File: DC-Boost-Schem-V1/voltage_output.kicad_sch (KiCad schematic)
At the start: 12 parts, among them Q5 HCNR200-300E, U11 MCP6007, U12 MCP6007

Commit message: Worked on layout
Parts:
- renumbered C40 to C59, C41 to C60, C42 to C61, C43 to C62, Q5 to Q8, R28 to R43, R29 to R44, R30 to R45, R31 to R46, R32 to R47, U11 to U17, U12 to U18
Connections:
- net GNDD renamed GND

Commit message: Layout update
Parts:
- R46: footprint Resistor_SMD:R_0805_2012Metric -> Resistor_SMD:R_0603_1608Metric
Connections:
- net GNDPWR renamed GNDREF
- net GNDREF: no longer C59.1, U17.4 (V-)
- new net: C59.1, U17.4 (V-)

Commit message: update
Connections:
- net GNDREF: now also C59.1, U17.4 (V-)
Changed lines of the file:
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@@
+	)
+	(symbol
+		(lib_id "power:GNDREF")
+		(at 134.62 74.93 0)
+		(unit 1)
+		(exclude_from_sim no)
+		(in_bom yes)
+		(on_board yes)
+		(dnp no)
+		(fields_autoplaced yes)
+		(property "Reference" "#PWR0501"
+			(at 134.62 81.28 0)
+			(effects
+				(font
+					(size 1.27 1.27)
+				)
+				(hide yes)
+			)
+		)
+		(property "Value" "GNDREF"
+			(at 134.62 80.01 0)
+			(effects
+				(font
+					(size 1.27 1.27)
+				)
+			)
+		)
+		(property "Footprint" ""
+			(at 134.62 74.93 0)
+			(effects
+				(font
+					(size 1.27 1.27)
+				)
+				(hide yes)
+			)
+		)
+		(property "Datasheet" ""
+			(at 134.62 74.93 0)
+			(effects
+				(font
+					(size 1.27 1.27)
+				)
+				(hide yes)
+			)
+		)
+		(property "Description" "Power symbol creates a global label with name \"GNDREF\" , reference supply ground"
+			(at 134.62 74.93 0)
+			(effects
+				(font
+					(size 1.27 1.27)
+				)
+				(hide yes)
+			)
+		)
+		(pin "1"
+		)
+		(instances
+			(project "DC-DC-Boost-V1"
+				(path "/892bc44b-f7f8-4677-bf53-06d5523b6450/75fe99dd-6331-41c4-aaf2-0a4fa01a955e"
+					(reference "#PWR0501")
+					(unit 1)
+				)
+			)
+		)
 	)
 	(symbol

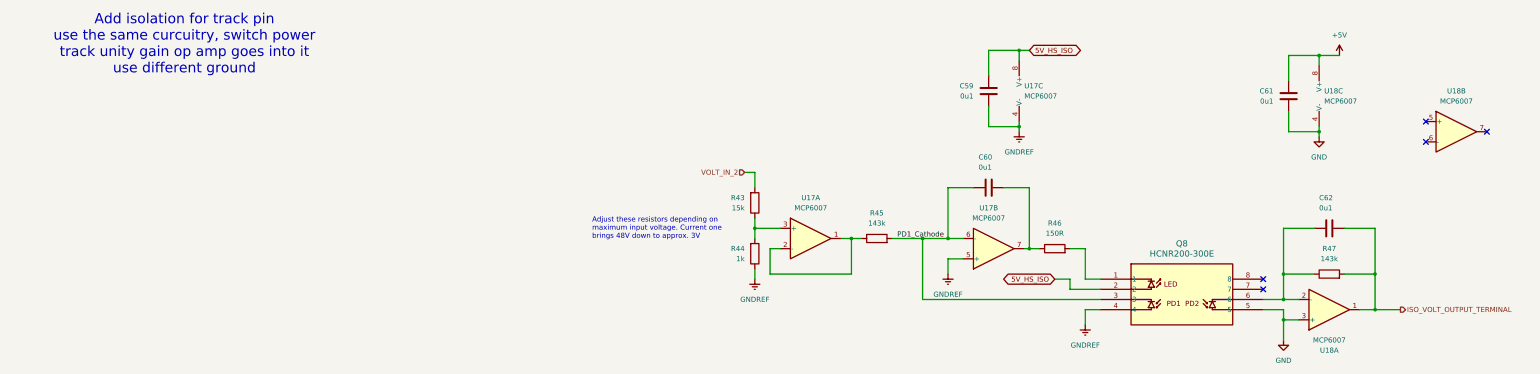
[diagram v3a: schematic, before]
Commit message: More layout and routing
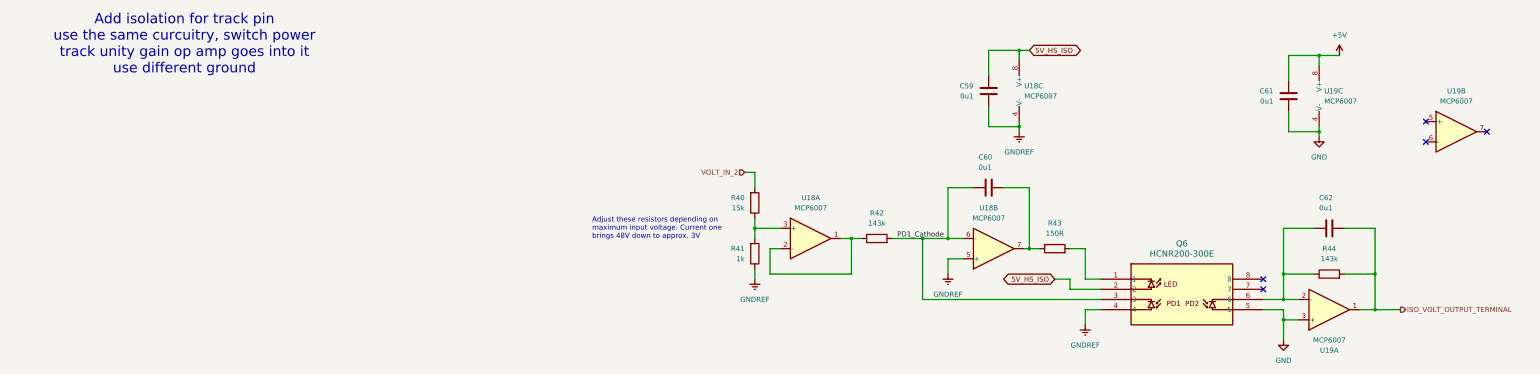
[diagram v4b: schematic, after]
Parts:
- renumbered Q8 to Q6, R43 to R40, R44 to R41, R45 to R42, R46 to R43, R47 to R44, U17 to U18, U18 to U19
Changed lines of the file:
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@@
 		(dnp no)
 		(fields_autoplaced yes)
-		(property "Reference" "#PWR079"
+		(property "Reference" "#PWR078"
 			(at 116.84 116.84 0)
 			(effects
@@
 			(project "DC-DC-Boost-V1"
 				(path "/892bc44b-f7f8-4677-bf53-06d5523b6450/75fe99dd-6331-41c4-aaf2-0a4fa01a955e"
-					(reference "#PWR079")
+					(reference "#PWR078")
 					(unit 1)
 				)
@@
 		(dnp no)
 		(fields_autoplaced yes)
-		(property "Reference" "Q8"
+		(property "Reference" "Q6"
 			(at 175.26 102.87 0)
 			(effects
@@
 			(project "DC-DC-Boost-V1"
 				(path "/892bc44b-f7f8-4677-bf53-06d5523b6450/75fe99dd-6331-41c4-aaf2-0a4fa01a955e"
-					(reference "Q8")
+					(reference "Q6")
 					(unit 1)
 				)
@@
 		(dnp no)
 		(fields_autoplaced yes)
-		(property "Reference" "R46"
+		(property "Reference" "R43"
 			(at 143.51 97.79 90)
 			(effects
@@
 			(project "DC-DC-Boost-V1"
 				(path "/892bc44b-f7f8-4677-bf53-06d5523b6450/75fe99dd-6331-41c4-aaf2-0a4fa01a955e"
-					(reference "R46")
+					(reference "R43")
 					(unit 1)
 				)
@@
 		(dnp no)
 		(fields_autoplaced yes)
-		(property "Reference" "#PWR085"
+		(property "Reference" "#PWR083"
 			(at 214.63 59.69 0)
 			(effects
@@
 			(project "DC-DC-Boost-V1"
 				(path "/892bc44b-f7f8-4677-bf53-06d5523b6450/75fe99dd-6331-41c4-aaf2-0a4fa01a955e"
-					(reference "#PWR085")
+					(reference "#PWR083")
 					(unit 1)
 				)
@@
 		(dnp no)
 		(fields_autoplaced yes)
-		(property "Reference" "#PWR099"
+		(property "Reference" "#PWR081"
 			(at 200.66 133.35 0)
 			(effects
@@
 			(project "DC-DC-Boost-V1"
 				(path "/892bc44b-f7f8-4677-bf53-06d5523b6450/75fe99dd-6331-41c4-aaf2-0a4fa01a955e"
-					(reference "#PWR099")
+					(reference "#PWR081")
 					(unit 1)
 				)
@@
 		(dnp no)
 		(fields_autoplaced yes)
-		(property "Reference" "R47"
+		(property "Reference" "R44"
 			(at 212.09 104.14 90)
 			(effects
@@
 			(project "DC-DC-Boost-V1"
 				(path "/892bc44b-f7f8-4677-bf53-06d5523b6450/75fe99dd-6331-41c4-aaf2-0a4fa01a955e"
-					(reference "R47")
+					(reference "R44")
 					(unit 1)
 				)
@@
 		(dnp no)
 		(fields_autoplaced yes)
-		(property "Reference" "#PWR0501"
+		(property "Reference" "#PWR079"
 			(at 134.62 81.28 0)
 			(effects
@@
 			(project "DC-DC-Boost-V1"
 				(path "/892bc44b-f7f8-4677-bf53-06d5523b6450/75fe99dd-6331-41c4-aaf2-0a4fa01a955e"
-					(reference "#PWR0501")
+					(reference "#PWR079")
 					(unit 1)
 				)
@@
 		(dnp no)
 		(fields_autoplaced yes)
-		(property "Reference" "U18"
+		(property "Reference" "U19"
 			(at 243.84 64.77 0)
 			(effects
@@
 			(project "DC-DC-Boost-V1"
 				(path "/892bc44b-f7f8-4677-bf53-06d5523b6450/75fe99dd-6331-41c4-aaf2-0a4fa01a955e"
-					(reference "U18")
+					(reference "U19")
 					(unit 2)
 				)
@@
 		(on_board yes)
 		(dnp no)
-		(property "Reference" "U18"
+		(property "Reference" "U19"
 			(at 212.09 129.54 0)
 			(effects
@@
 			(project "DC-DC-Boost-V1"
 				(path "/892bc44b-f7f8-4677-bf53-06d5523b6450/75fe99dd-6331-41c4-aaf2-0a4fa01a955e"
-					(reference "U18")
+					(reference "U19")
 					(unit 1)
 				)
@@
 		(dnp no)
 		(fields_autoplaced yes)
-		(property "Reference" "#PWR077"
+		(property "Reference" "#PWR082"
 			(at 209.55 82.55 0)
 			(effects
@@
 			(project "DC-DC-Boost-V1"
 				(path "/892bc44b-f7f8-4677-bf53-06d5523b6450/75fe99dd-6331-41c4-aaf2-0a4fa01a955e"
-					(reference "#PWR077")
+					(reference "#PWR082")
 					(unit 1)
 				)
@@
 		(dnp no)
 		(fields_autoplaced yes)
-		(property "Reference" "U18"
+		(property "Reference" "U19"
 			(at 210.82 64.7699 0)
 			(effects
@@
 			(project "DC-DC-Boost-V1"
 				(path "/892bc44b-f7f8-4677-bf53-06d5523b6450/75fe99dd-6331-41c4-aaf2-0a4fa01a955e"
-					(reference "U18")
+					(reference "U19")
 					(unit 3)
 				)
@@
 		(on_board yes)
 		(dnp no)
-		(property "Reference" "U17"
+		(property "Reference" "U18"
 			(at 127 93.98 0)
 			(effects
@@
 			(project "DC-DC-Boost-V1"
 				(path "/892bc44b-f7f8-4677-bf53-06d5523b6450/75fe99dd-6331-41c4-aaf2-0a4fa01a955e"
-					(reference "U17")
+					(reference "U18")
 					(unit 2)
 				)
@@
 		(dnp no)
 		(fields_autoplaced yes)
-		(property "Reference" "#PWR064"
+		(property "Reference" "#PWR077"
 			(at 68.58 118.11 0)
 			(effects
@@
 			(project "DC-DC-Boost-V1"
 				(path "/892bc44b-f7f8-4677-bf53-06d5523b6450/75fe99dd-6331-41c4-aaf2-0a4fa01a955e"
-					(reference "#PWR064")
+					(reference "#PWR077")
 					(unit 1)
 				)
@@
 		(on_board yes)
 		(dnp no)
-		(property "Reference" "R44"
+		(property "Reference" "R41"
 			(at 66.04 104.1399 0)
 			(effects
@@
 			(project "DC-DC-Boost-V1"
 				(path "/892bc44b-f7f8-4677-bf53-06d5523b6450/75fe99dd-6331-41c4-aaf2-0a4fa01a955e"
-					(reference "R44")
+					(reference "R41")
 					(unit 1)
 				)
@@
 		(dnp no)
 		(fields_autoplaced yes)
-		(property "Reference" "R45"
+		(property "Reference" "R42"
 			(at 99.06 95.25 90)
 			(effects
@@
 			(project "DC-DC-Boost-V1"
 				(path "/892bc44b-f7f8-4677-bf53-06d5523b6450/75fe99dd-6331-41c4-aaf2-0a4fa01a955e"
-					(reference "R45")
+					(reference "R42")
 					(unit 1)
 				)
@@
 		(on_board yes)
 		(dnp no)
-		(property "Reference" "R43"
+		(property "Reference" "R40"
 			(at 66.04 91.4399 0)
 			(effects
@@
 			(project "DC-DC-Boost-V1"
 				(path "/892bc44b-f7f8-4677-bf53-06d5523b6450/75fe99dd-6331-41c4-aaf2-0a4fa01a955e"
-					(reference "R43")
+					(reference "R40")
 					(unit 1)
 				)
@@
 		(dnp no)
 		(fields_autoplaced yes)
-		(property "Reference" "U17"
+		(property "Reference" "U18"
 			(at 82.55 91.44 0)
 			(effects
@@
 			(project "DC-DC-Boost-V1"
 				(path "/892bc44b-f7f8-4677-bf53-06d5523b6450/75fe99dd-6331-41c4-aaf2-0a4fa01a955e"
-					(reference "U17")
+					(reference "U18")
 					(unit 1)
 				)
@@
 		(dnp no)
 		(fields_autoplaced yes)
-		(property "Reference" "U17"
+		(property "Reference" "U18"
 			(at 135.89 63.4999 0)
 			(effects
@@
 			(project "DC-DC-Boost-V1"
 				(path "/892bc44b-f7f8-4677-bf53-06d5523b6450/75fe99dd-6331-41c4-aaf2-0a4fa01a955e"
-					(reference "U17")
+					(reference "U18")
 					(unit 3)
 				)

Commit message: Added more to layout
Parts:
- renumbered C59 to C62, C60 to C63, C61 to C64, C62 to C65, R40 to R42, R41 to R43, R42 to R44, R43 to R45, R44 to R46
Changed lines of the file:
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@@
 		(on_board yes)
 		(dnp no)
-		(property "Reference" "C60"
+		(property "Reference" "C63"
 			(at 124.46 81.28 90)
 			(effects
@@
 			(project "DC-DC-Boost-V1"
 				(path "/892bc44b-f7f8-4677-bf53-06d5523b6450/75fe99dd-6331-41c4-aaf2-0a4fa01a955e"
-					(reference "C60")
+					(reference "C63")
 					(unit 1)
 				)
@@
 		(on_board yes)
 		(dnp no)
-		(property "Reference" "C61"
+		(property "Reference" "C64"
 			(at 198.12 64.77 0)
 			(effects
@@
 			(project "DC-DC-Boost-V1"
 				(path "/892bc44b-f7f8-4677-bf53-06d5523b6450/75fe99dd-6331-41c4-aaf2-0a4fa01a955e"
-					(reference "C61")
+					(reference "C64")
 					(unit 1)
 				)
@@
 		(on_board yes)
 		(dnp no)
-		(property "Reference" "C59"
+		(property "Reference" "C62"
 			(at 123.19 63.5 0)
 			(effects
@@
 			(project "DC-DC-Boost-V1"
 				(path "/892bc44b-f7f8-4677-bf53-06d5523b6450/75fe99dd-6331-41c4-aaf2-0a4fa01a955e"
-					(reference "C59")
+					(reference "C62")
 					(unit 1)
 				)
@@
 		(dnp no)
 		(fields_autoplaced yes)
-		(property "Reference" "R43"
+		(property "Reference" "R45"
 			(at 143.51 97.79 90)
 			(effects
@@
 			(project "DC-DC-Boost-V1"
 				(path "/892bc44b-f7f8-4677-bf53-06d5523b6450/75fe99dd-6331-41c4-aaf2-0a4fa01a955e"
-					(reference "R43")
+					(reference "R45")
 					(unit 1)
 				)
@@
 		(dnp no)
 		(fields_autoplaced yes)
-		(property "Reference" "R44"
+		(property "Reference" "R46"
 			(at 212.09 104.14 90)
 			(effects
@@
 			(project "DC-DC-Boost-V1"
 				(path "/892bc44b-f7f8-4677-bf53-06d5523b6450/75fe99dd-6331-41c4-aaf2-0a4fa01a955e"
-					(reference "R44")
+					(reference "R46")
 					(unit 1)
 				)
@@
 		(on_board yes)
 		(dnp no)
-		(property "Reference" "C62"
+		(property "Reference" "C65"
 			(at 209.55 91.44 90)
 			(effects
@@
 			(project "DC-DC-Boost-V1"
 				(path "/892bc44b-f7f8-4677-bf53-06d5523b6450/75fe99dd-6331-41c4-aaf2-0a4fa01a955e"
-					(reference "C62")
+					(reference "C65")
 					(unit 1)
 				)
@@
 		(on_board yes)
 		(dnp no)
-		(property "Reference" "R41"
+		(property "Reference" "R43"
 			(at 66.04 104.1399 0)
 			(effects
@@
 			(project "DC-DC-Boost-V1"
 				(path "/892bc44b-f7f8-4677-bf53-06d5523b6450/75fe99dd-6331-41c4-aaf2-0a4fa01a955e"
-					(reference "R41")
+					(reference "R43")
 					(unit 1)
 				)
@@
 		(dnp no)
 		(fields_autoplaced yes)
-		(property "Reference" "R42"
+		(property "Reference" "R44"
 			(at 99.06 95.25 90)
 			(effects
@@
 			(project "DC-DC-Boost-V1"
 				(path "/892bc44b-f7f8-4677-bf53-06d5523b6450/75fe99dd-6331-41c4-aaf2-0a4fa01a955e"
-					(reference "R42")
+					(reference "R44")
 					(unit 1)
 				)
@@
 		(on_board yes)
 		(dnp no)
-		(property "Reference" "R40"
+		(property "Reference" "R42"
 			(at 66.04 91.4399 0)
 			(effects
@@
 			(project "DC-DC-Boost-V1"
 				(path "/892bc44b-f7f8-4677-bf53-06d5523b6450/75fe99dd-6331-41c4-aaf2-0a4fa01a955e"
-					(reference "R40")
-					(unit 1)
-				)
+					(reference "R42")
+					(unit 1)
+				)

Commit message: updated code
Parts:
- R42: value 15k -> 20k
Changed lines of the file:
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@@
 			)
 		)
-		(property "Value" "15k"
+		(property "Value" "20k"
 			(at 66.04 93.9799 0)
 			(effects
